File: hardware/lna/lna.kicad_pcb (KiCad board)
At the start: 2 copper layers, 6 parts, among them J1 142-0701-801, J2 142-0701-801, U1 BGU7007,115

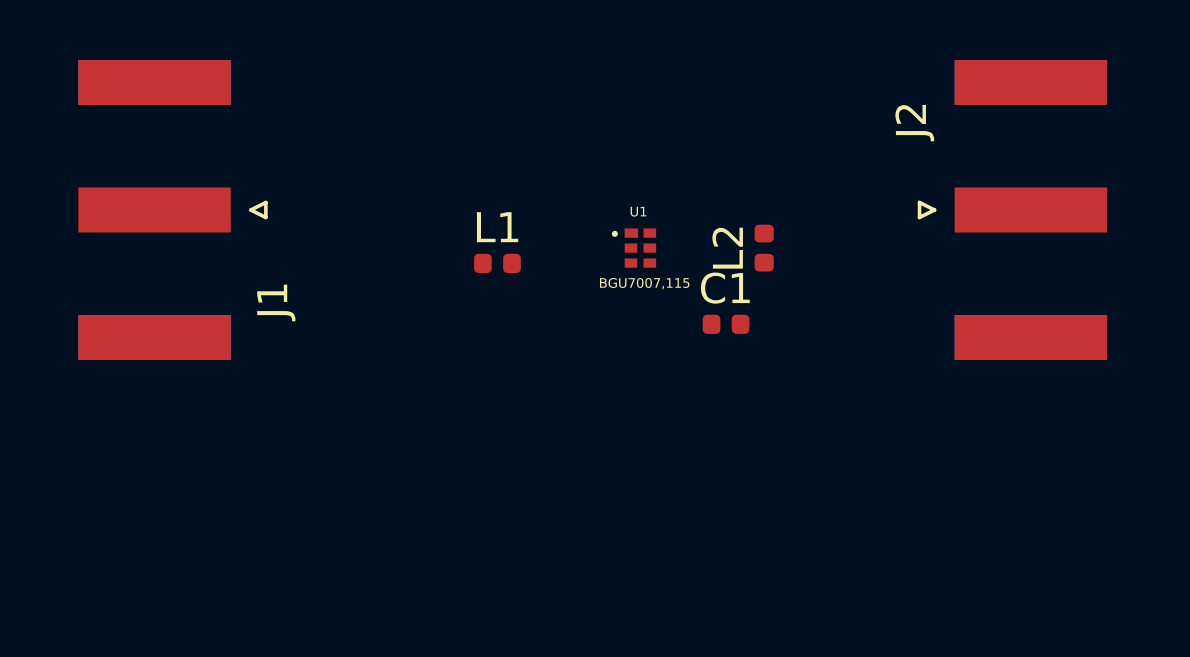
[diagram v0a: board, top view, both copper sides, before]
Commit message: completed schematic and laid out PCB
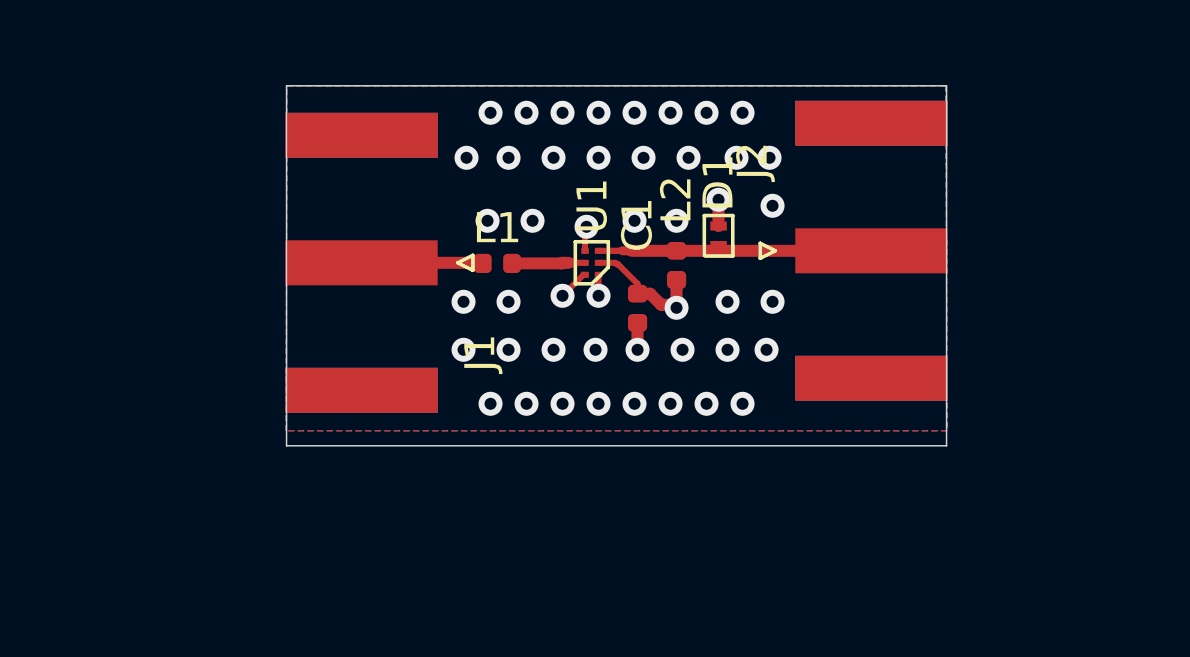
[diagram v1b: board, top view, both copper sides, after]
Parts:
- added D1: Bi_ESD_Diode, lna:SOIC-2, F.Cu at (183.9, 105.0)
- U1: value BGU7007,115 -> BGU8009; footprint BGU7007_115:PSON50P100X145X50-6N -> Package_TO_SOT_SMD:XSON-NXP-6
- moved J1 7.12 mm to (172.0, 105.9)
- moved J2 5.48 mm to (189.0, 105.5)
- moved C1 3.00 mm to (181.2, 107.4), turned to 90 degrees
- moved L2 2.98 mm to (182.5, 106.0)
- moved U1 1.69 mm to (179.7, 105.9), turned to 90 degrees
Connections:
- C1 pad 1: GND -> GNDA
- J2 pad 1: Net-(J2-Pad1) -> Net-(D1-Pad1)
- L2 pad 2: Net-(J2-Pad1) -> Net-(D1-Pad1)
- U1 pad 2: GNDA -> VCC
- U1 pad 3: Net-(L1-Pad2) -> Net-(D1-Pad1)
- U1 pad 4: VCC -> GNDA
- U1 pad 5: VCC -> Net-(L1-Pad2)
- U1 pad 6: Net-(J2-Pad1) -> VCC
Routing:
- net Net-(D1-Pad1): track 0.00 -> 9.60 mm
- net VCC: track 0.00 -> 5.38 mm, vias 0 -> 2
- net Net-(J1-Pad1): track 0.00 -> 4.05 mm
- net GNDA: track 0.00 -> 3.30 mm, vias 0 -> 44
- net Net-(L1-Pad2): track 0.00 -> 2.44 mm
- added copper zone on B.Cu, net GNDA
- added copper zone on F.Cu, net GNDA
- added copper zone on In1.Cu, net GNDA
- added copper zone on In2.Cu, net VCC
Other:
- board outline added: 22 x 12 mm
- copper layers 2 -> 4

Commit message: changed connectors and added 3d stuff
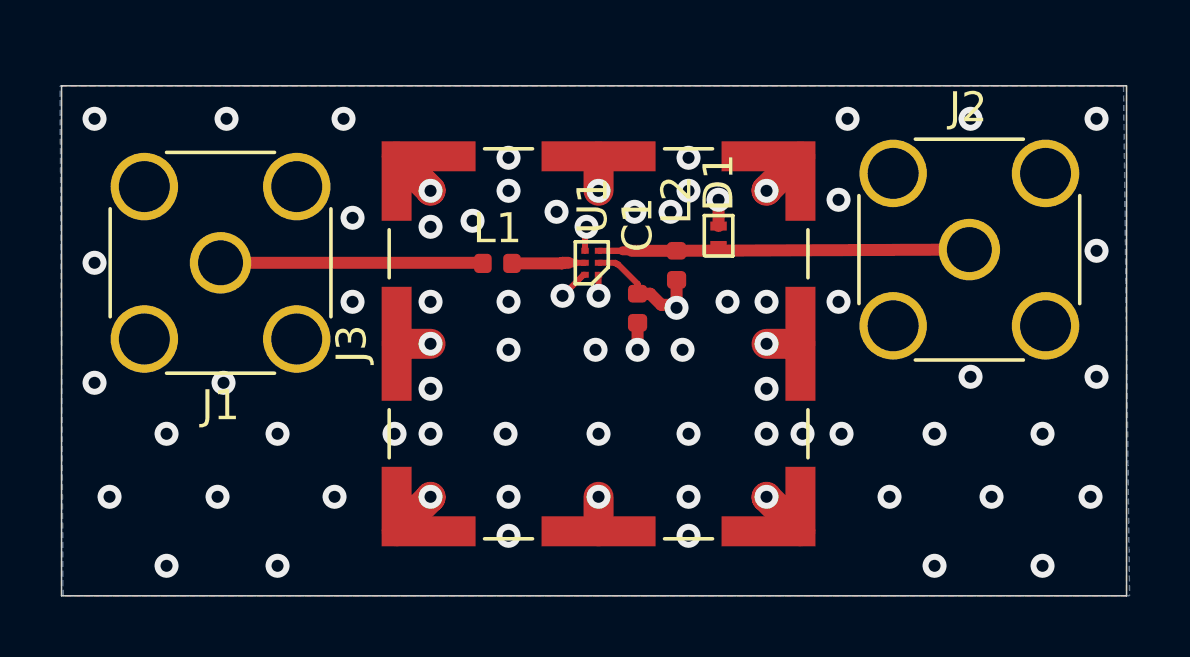
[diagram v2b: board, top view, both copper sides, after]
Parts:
- added J3: Conn_01x01_Male, RF_Shielding:Laird_Technologies_BMI-S-101_13.66x12.70mm, F.Cu at (179.9, 108.6)
- J1, J2: footprint Connector_Coaxial:SMA_Amphenol_132289_EdgeMount -> Connector_Coaxial:SMA_Amphenol_132134_Vertical
- moved J1 4.70 mm to (167.3, 105.9)
- moved J2 3.26 mm to (192.3, 105.5), turned to 180 degrees
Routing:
- net GNDA: track 3.30 -> 14.3 mm, vias 44 -> 72
- net Net-(J1-Pad1): track 4.05 -> 8.75 mm
- net Net-(D1-Pad1): track 9.60 -> 12.9 mm
- added copper zone on In2.Cu, net GNDA
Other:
- board size 22 x 12 mm -> 35.5 x 17 mm
- board text added: "TART-3 Low Noise Antenna Amplifier (c)2019 4i Systems"

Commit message: Add shield and mounting holes
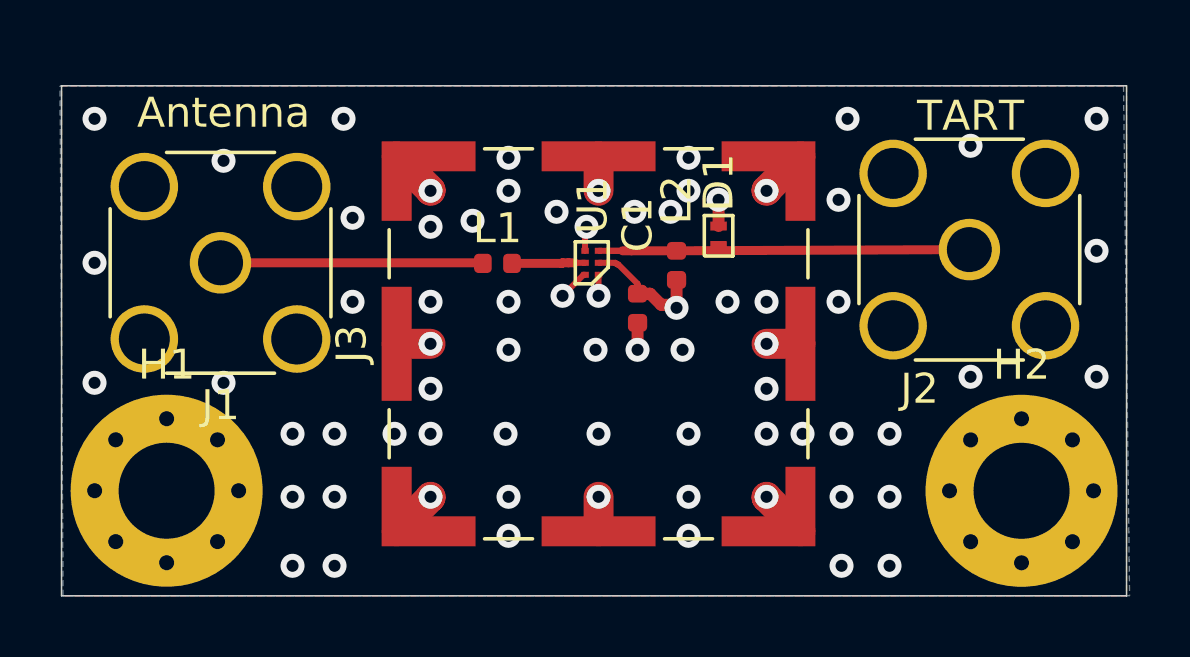
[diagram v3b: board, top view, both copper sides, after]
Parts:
- added H1: MountingHole_Pad, MountingHole:MountingHole_3.2mm_M3_Pad_Via, F.Cu at (165.5, 113.5)
- added H2: MountingHole_Pad, MountingHole:MountingHole_3.2mm_M3_Pad_Via, F.Cu at (194.0, 113.5)
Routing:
- net GNDA: vias 72 -> 69
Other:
- board text added: "Antenna"
- board text added: "TART"

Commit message: Preliminary radio module schematic
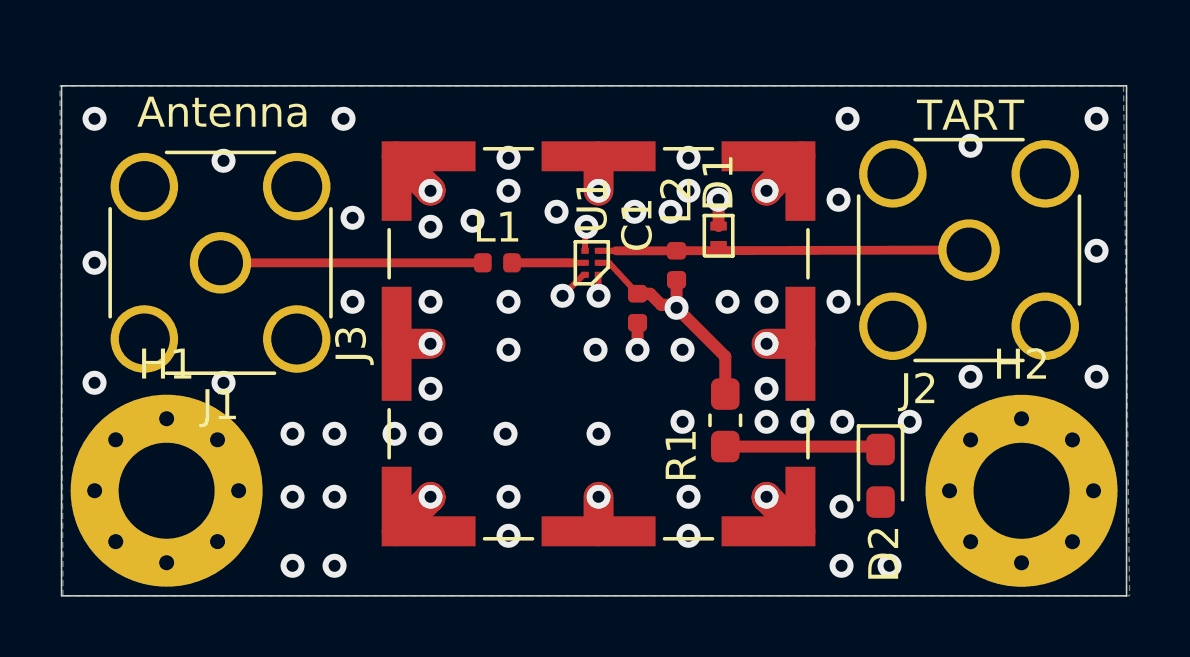
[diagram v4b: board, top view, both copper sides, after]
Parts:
- added D2: PWR, LED_SMD:LED_0603_1608Metric_Pad1.05x0.95mm_HandSolder, F.Cu at (189.3, 113.0)
- added R1: 1K, Resistor_SMD:R_0603_1608Metric_Pad1.05x0.95mm_HandSolder, F.Cu at (184.1, 111.2)
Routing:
- net Net-(D2-Pad1): track 0.00 -> 5.22 mm
- net VCC: track 5.38 -> 8.76 mm
- net GNDA: vias 69 -> 68

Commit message: added development board
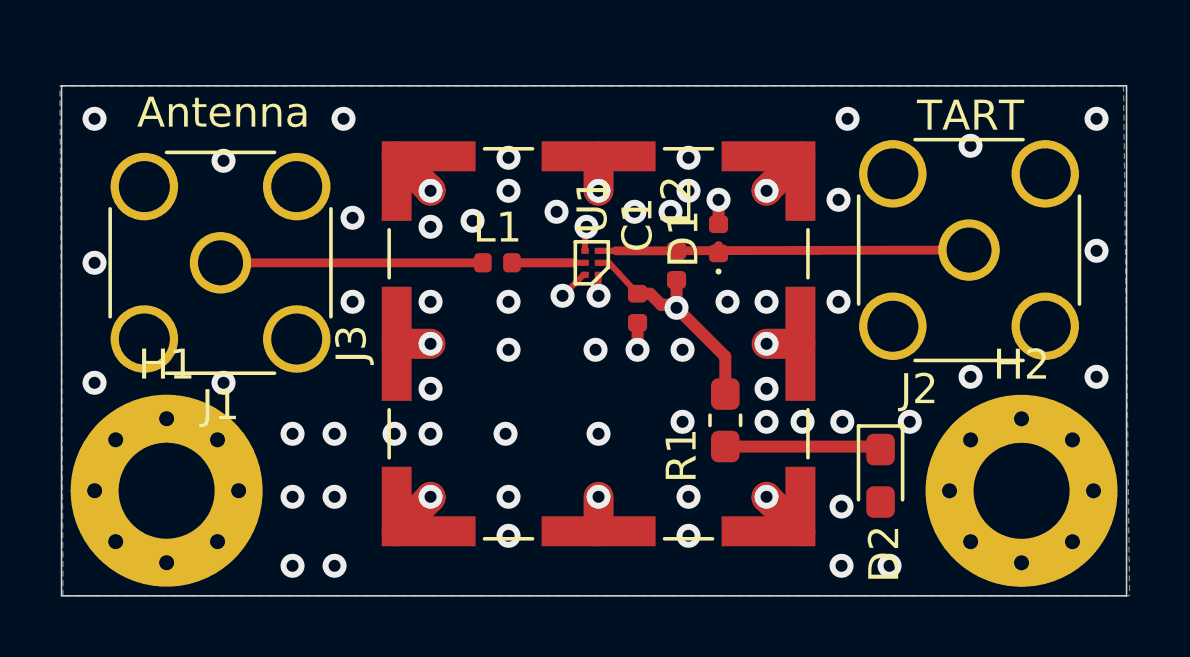
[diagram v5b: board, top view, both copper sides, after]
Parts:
- D1: footprint lna:SOIC-2 -> Diode_SMD:D_0402_1005Metric
- moved D1 0.10 mm to (183.9, 105.1), turned to 90 degrees
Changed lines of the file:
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@@
-(kicad_pcb (version 20171130) (host pcbnew 5.1.4+dfsg1-1)
+(kicad_pcb (version 20171130) (host pcbnew 5.1.4+dfsg1-2)
   (general
     (thickness 1)
@@
   )
   (setup
-    (last_trace_width 0.4)
+    (last_trace_width 0.25)
     (user_trace_width 0.2)
     (user_trace_width 0.3)
@@
     (add_net VCC)
   )
+  (module Diode_SMD:D_0402_1005Metric (layer F.Cu)
+    (at 183.9 105.1 90)
+    (descr "Diode SMD 0402 (1005 Metric), square (rectangular) end terminal, IPC_7351 nominal, (Body size source: http://www.tortai-tech.com/upload/download/2011102023233369053.pdf), generated with kicad-footprint-generator")
+    (tags diode)
+    (attr smd)
+    (fp_text reference D1 (at 0 -1.17 90) (layer F.SilkS)
+      (effects (font (size 1 1) (thickness 0.15)))
+    )
+    (fp_text value Bi_ESD_Diode (at 0 1.17 90) (layer F.Fab)
+      (effects (font (size 1 1) (thickness 0.15)))
+    )
+    (fp_text user %R (at 0 0 90) (layer F.Fab)
+      (effects (font (size 0.25 0.25) (thickness 0.04)))
+    )
+    (fp_line (start 0.93 0.47) (end -0.93 0.47) (layer F.CrtYd) (width 0.05))
+    (fp_line (start 0.93 -0.47) (end 0.93 0.47) (layer F.CrtYd) (width 0.05))
+    (fp_line (start -0.93 -0.47) (end 0.93 -0.47) (layer F.CrtYd) (width 0.05))
+    (fp_line (start -0.93 0.47) (end -0.93 -0.47) (layer F.CrtYd) (width 0.05))
+    (fp_line (start -0.3 0.25) (end -0.3 -0.25) (layer F.Fab) (width 0.1))
+    (fp_line (start -0.4 0.25) (end -0.4 -0.25) (layer F.Fab) (width 0.1))
+    (fp_line (start 0.5 0.25) (end -0.5 0.25) (layer F.Fab) (width 0.1))
+    (fp_line (start 0.5 -0.25) (end 0.5 0.25) (layer F.Fab) (width 0.1))
+    (fp_line (start -0.5 -0.25) (end 0.5 -0.25) (layer F.Fab) (width 0.1))
+    (fp_line (start -0.5 0.25) (end -0.5 -0.25) (layer F.Fab) (width 0.1))
+    (fp_circle (center -1.09 0) (end -1.04 0) (layer F.SilkS) (width 0.1))
+    (pad 2 smd roundrect (at 0.485 0 90) (size 0.59 0.64) (layers F.Cu F.Paste F.Mask) (roundrect_rratio 0.25)
+      (net 3 GNDA))
+    (pad 1 smd roundrect (at -0.485 0 90) (size 0.59 0.64) (layers F.Cu F.Paste F.Mask) (roundrect_rratio 0.25)
+      (net 5 "Net-(D1-Pad1)"))
+    (model ${KISYS3DMOD}/Diode_SMD.3dshapes/D_0402_1005Metric.wrl
+      (at (xyz 0 0 0))
+      (scale (xyz 1 1 1))
+      (rotate (xyz 0 0 0))
+    )
+  )
   (module Resistor_SMD:R_0603_1608Metric_Pad1.05x0.95mm_HandSolder (layer F.Cu)
     (at 184.125 111.15 270)
@@
     )
   )
-  (module lna:SOIC-2 (layer F.Cu)
-    (at 183.9 105)
-    (attr smd)
-    (fp_text reference D1 (at 0 -1.775 90) (layer F.SilkS)
-      (effects (font (size 1 1) (thickness 0.15)))
-    )
-    (fp_text value Bi_ESD_Diode (at 0 0) (layer F.Fab) hide
-      (effects (font (size 1 1) (thickness 0.15)))
-    )
-    (fp_line (start -0.52 0.72) (end -0.52 -0.72) (layer F.CrtYd) (width 0.05))
-    (fp_line (start 0.52 0.72) (end -0.52 0.72) (layer F.CrtYd) (width 0.05))
-    (fp_line (start 0.52 -0.72) (end 0.52 0.72) (layer F.CrtYd) (width 0.05))
-    (fp_line (start -0.52 -0.72) (end 0.52 -0.72) (layer F.CrtYd) (width 0.05))
-    (fp_line (start 0.475 0.675) (end -0.45 0.675) (layer F.SilkS) (width 0.12))
-    (fp_line (start 0.475 -0.675) (end 0.475 0.675) (layer F.SilkS) (width 0.12))
-    (fp_line (start -0.475 -0.675) (end 0.475 -0.675) (layer F.SilkS) (width 0.12))
-    (fp_line (start -0.475 0.65) (end -0.475 -0.675) (layer F.SilkS) (width 0.12))
-    (pad 1 smd rect (at 0 0.325) (size 0.55 0.3) (layers F.Cu F.Paste F.Mask)
-      (net 5 "Net-(D1-Pad1)"))
-    (pad 2 smd rect (at 0 -0.325) (size 0.55 0.3) (layers F.Cu F.Paste F.Mask)
-      (net 3 GNDA))
-    (model ${KISYS3DMOD}/Diode_SMD.3dshapes/D_SOD-523.wrl
-      (at (xyz 0 0 0))
-      (scale (xyz 1 1 1))
-      (rotate (xyz 0 0 90))
-    )
-  )
